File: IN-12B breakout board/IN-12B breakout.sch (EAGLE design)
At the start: 25 parts, among them Q1 500mA/300V, Q10 500mA/300V, Q2 500mA/300V, Q3 500mA/300V, Q4 500mA/300V, Q5 500mA/300V, Q6 500mA/300V, Q7 500mA/300V, Q8 500mA/300V, Q9 500mA/300V

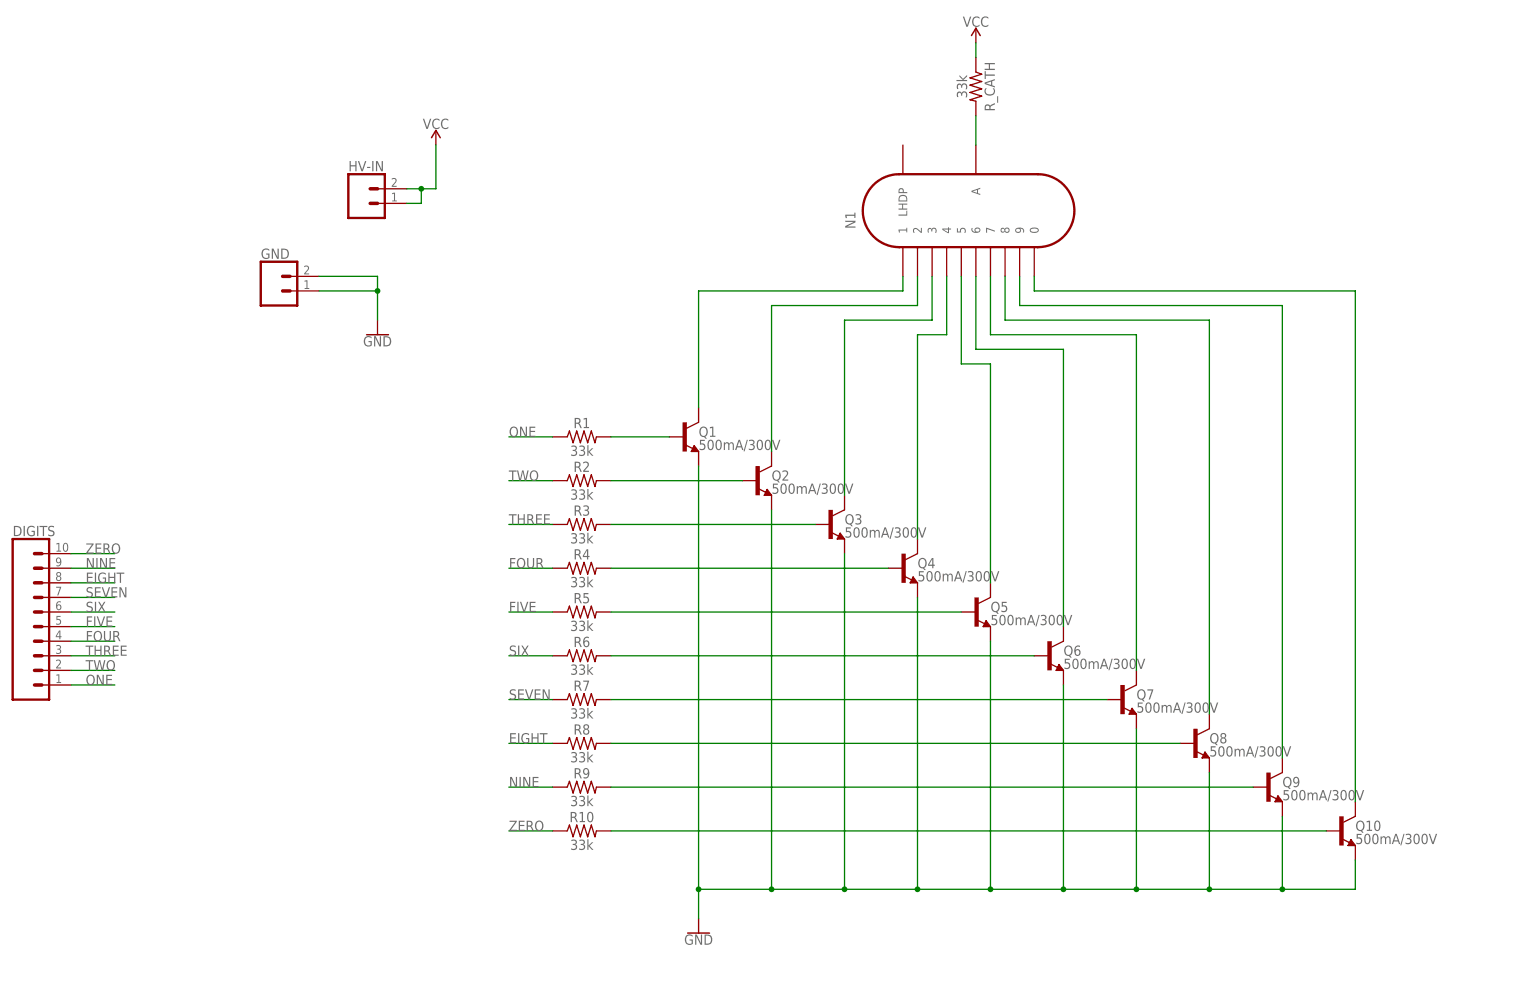
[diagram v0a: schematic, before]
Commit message: board version 2.0, with decimal dot support
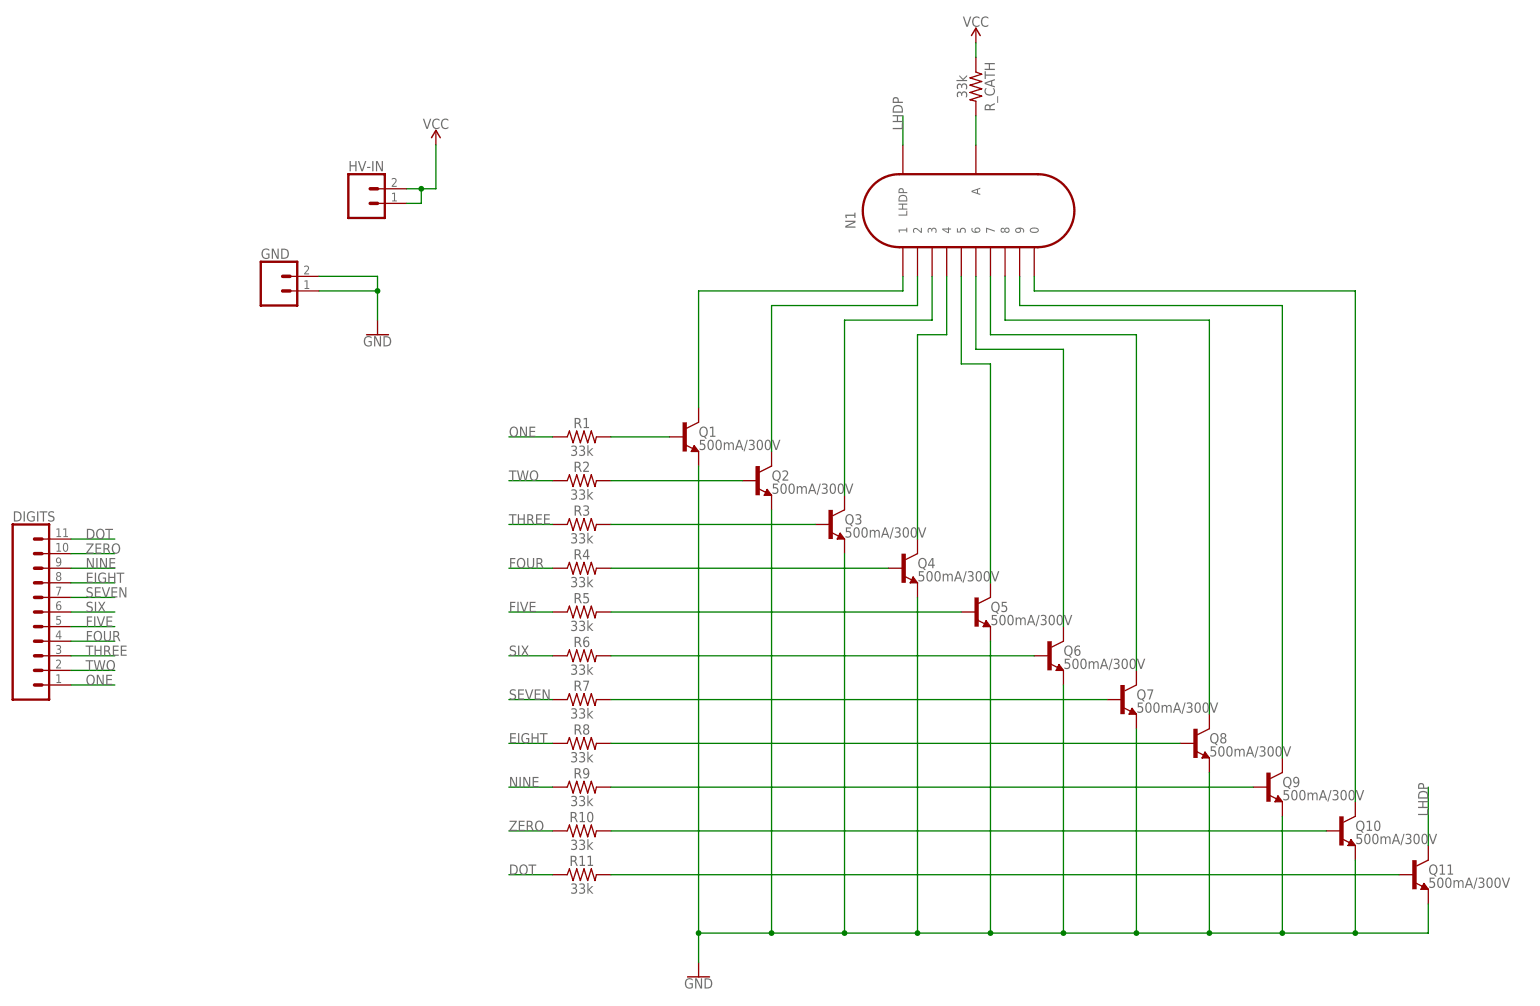
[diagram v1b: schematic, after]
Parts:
- added Q11: 500mA/300V, SparkFun-DiscreteSemi:TRANS_NPN-MMBTA42
- added R11: 33k, SparkFun-Resistors:33KOHM-0603-1/10W-1%
- DIGITS: device SparkFun-Connectors:CONN_10" -> SparkFun-Connectors:CONN_11
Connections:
- new net DOT: DIGITS.11, R11.1
- new net LHDP: N1.LHDP, Q11.C
- new net N$22: Q11.B, R11.2
- net GND: now also Q11.E
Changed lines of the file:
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@@
 <part name="SUPPLY2" library="SparkFun-PowerSymbols" deviceset="VCC" device=""/>
 <part name="R_CATH" library="SparkFun-Resistors" deviceset="33KOHM" device="-0603-1/10W-1%" value="33k"/>
-<part name="DIGITS" library="SparkFun-Connectors" deviceset="CONN_10" device="&quot;"/>
+<part name="DIGITS" library="SparkFun-Connectors" deviceset="CONN_11" device=""/>
 <part name="N1" library="russian-nixies" deviceset="IN-12B" device=""/>
 <part name="GND" library="SparkFun-Connectors" deviceset="CONN_02" device=""/>
 <part name="GND2" library="SparkFun-PowerSymbols" deviceset="GND" device=""/>
+<part name="R11" library="SparkFun-Resistors" deviceset="33KOHM" device="-0603-1/10W-1%" value="33k"/>
+<part name="Q11" library="SparkFun-DiscreteSemi" deviceset="TRANS_NPN" device="-MMBTA42" value="500mA/300V"/>
 </parts>
 <sheets>
@@
 </plain>
 <instances>
-<instance part="GND1" gate="1" x="-17.78" y="10.16"/>
+<instance part="GND1" gate="1" x="-17.78" y="2.54"/>
 <instance part="Q1" gate="G$1" x="-20.32" y="96.52"/>
 <instance part="Q2" gate="G$1" x="-7.62" y="88.9"/>
@@
 <instance part="SUPPLY2" gate="G$1" x="30.48" y="165.1"/>
 <instance part="R_CATH" gate="G$1" x="30.48" y="157.48" rot="R270"/>
-<instance part="DIGITS" gate="G$1" x="-137.16" y="71.12"/>
+<instance part="DIGITS" gate="G$1" x="-137.16" y="66.04"/>
 <instance part="N1" gate="G$1" x="30.48" y="137.16" rot="R90"/>
 <instance part="GND" gate="G$1" x="-91.44" y="121.92"/>
 <instance part="GND2" gate="1" x="-73.66" y="114.3"/>
+<instance part="R11" gate="G$1" x="-38.1" y="20.32"/>
+<instance part="Q11" gate="G$1" x="106.68" y="20.32"/>
 </instances>
 <busses>
@@
 <pinref part="Q1" gate="G$1" pin="E"/>
 <pinref part="GND1" gate="1" pin="GND"/>
-<wire x1="-17.78" y1="91.44" x2="-17.78" y2="17.78" width="0.1524" layer="91"/>
+<wire x1="-17.78" y1="91.44" x2="-17.78" y2="10.16" width="0.1524" layer="91"/>
 <pinref part="Q10" gate="G$1" pin="E"/>
-<wire x1="-17.78" y1="17.78" x2="-17.78" y2="12.7" width="0.1524" layer="91"/>
-<wire x1="-17.78" y1="17.78" x2="-5.08" y2="17.78" width="0.1524" layer="91"/>
-<wire x1="-5.08" y1="17.78" x2="7.62" y2="17.78" width="0.1524" layer="91"/>
-<wire x1="7.62" y1="17.78" x2="20.32" y2="17.78" width="0.1524" layer="91"/>
-<wire x1="20.32" y1="17.78" x2="33.02" y2="17.78" width="0.1524" layer="91"/>
-<wire x1="33.02" y1="17.78" x2="45.72" y2="17.78" width="0.1524" layer="91"/>
-<wire x1="45.72" y1="17.78" x2="58.42" y2="17.78" width="0.1524" layer="91"/>
-<wire x1="58.42" y1="17.78" x2="71.12" y2="17.78" width="0.1524" layer="91"/>
-<wire x1="71.12" y1="17.78" x2="83.82" y2="17.78" width="0.1524" layer="91"/>
-<wire x1="83.82" y1="17.78" x2="96.52" y2="17.78" width="0.1524" layer="91"/>
-<wire x1="96.52" y1="17.78" x2="96.52" y2="22.86" width="0.1524" layer="91"/>
-<junction x="-17.78" y="17.78"/>
+<wire x1="-17.78" y1="10.16" x2="-17.78" y2="5.08" width="0.1524" layer="91"/>
+<wire x1="-17.78" y1="10.16" x2="-5.08" y2="10.16" width="0.1524" layer="91"/>
+<wire x1="-5.08" y1="10.16" x2="7.62" y2="10.16" width="0.1524" layer="91"/>
+<wire x1="7.62" y1="10.16" x2="20.32" y2="10.16" width="0.1524" layer="91"/>
+<wire x1="20.32" y1="10.16" x2="33.02" y2="10.16" width="0.1524" layer="91"/>
+<wire x1="33.02" y1="10.16" x2="45.72" y2="10.16" width="0.1524" layer="91"/>
+<wire x1="45.72" y1="10.16" x2="58.42" y2="10.16" width="0.1524" layer="91"/>
+<wire x1="58.42" y1="10.16" x2="71.12" y2="10.16" width="0.1524" layer="91"/>
+<wire x1="71.12" y1="10.16" x2="83.82" y2="10.16" width="0.1524" layer="91"/>
+<wire x1="83.82" y1="10.16" x2="96.52" y2="10.16" width="0.1524" layer="91"/>
+<wire x1="96.52" y1="10.16" x2="96.52" y2="22.86" width="0.1524" layer="91"/>
+<junction x="-17.78" y="10.16"/>
 <pinref part="Q9" gate="G$1" pin="E"/>
-<wire x1="83.82" y1="30.48" x2="83.82" y2="17.78" width="0.1524" layer="91"/>
-<junction x="83.82" y="17.78"/>
+<wire x1="83.82" y1="30.48" x2="83.82" y2="10.16" width="0.1524" layer="91"/>
+<junction x="83.82" y="10.16"/>
 <pinref part="Q8" gate="G$1" pin="E"/>
-<wire x1="71.12" y1="38.1" x2="71.12" y2="17.78" width="0.1524" layer="91"/>
-<junction x="71.12" y="17.78"/>
+<wire x1="71.12" y1="38.1" x2="71.12" y2="10.16" width="0.1524" layer="91"/>
+<junction x="71.12" y="10.16"/>
 <pinref part="Q7" gate="G$1" pin="E"/>
-<wire x1="58.42" y1="45.72" x2="58.42" y2="17.78" width="0.1524" layer="91"/>
-<junction x="58.42" y="17.78"/>
+<wire x1="58.42" y1="45.72" x2="58.42" y2="10.16" width="0.1524" layer="91"/>
+<junction x="58.42" y="10.16"/>
 <pinref part="Q6" gate="G$1" pin="E"/>
-<wire x1="45.72" y1="53.34" x2="45.72" y2="17.78" width="0.1524" layer="91"/>
-<junction x="45.72" y="17.78"/>
+<wire x1="45.72" y1="53.34" x2="45.72" y2="10.16" width="0.1524" layer="91"/>
+<junction x="45.72" y="10.16"/>
 <pinref part="Q5" gate="G$1" pin="E"/>
-<wire x1="33.02" y1="60.96" x2="33.02" y2="17.78" width="0.1524" layer="91"/>
-<junction x="33.02" y="17.78"/>
+<wire x1="33.02" y1="60.96" x2="33.02" y2="10.16" width="0.1524" layer="91"/>
+<junction x="33.02" y="10.16"/>
 <pinref part="Q4" gate="G$1" pin="E"/>
-<wire x1="20.32" y1="68.58" x2="20.32" y2="17.78" width="0.1524" layer="91"/>
-<junction x="20.32" y="17.78"/>
+<wire x1="20.32" y1="68.58" x2="20.32" y2="10.16" width="0.1524" layer="91"/>
+<junction x="20.32" y="10.16"/>
 <pinref part="Q3" gate="G$1" pin="E"/>
-<wire x1="7.62" y1="76.2" x2="7.62" y2="17.78" width="0.1524" layer="91"/>
-<junction x="7.62" y="17.78"/>
+<wire x1="7.62" y1="76.2" x2="7.62" y2="10.16" width="0.1524" layer="91"/>
+<junction x="7.62" y="10.16"/>
 <pinref part="Q2" gate="G$1" pin="E"/>
-<wire x1="-5.08" y1="83.82" x2="-5.08" y2="17.78" width="0.1524" layer="91"/>
-<junction x="-5.08" y="17.78"/>
+<wire x1="-5.08" y1="83.82" x2="-5.08" y2="10.16" width="0.1524" layer="91"/>
+<junction x="-5.08" y="10.16"/>
+<pinref part="Q11" gate="G$1" pin="E"/>
+<wire x1="109.22" y1="15.24" x2="109.22" y2="10.16" width="0.1524" layer="91"/>
+<wire x1="109.22" y1="10.16" x2="96.52" y2="10.16" width="0.1524" layer="91"/>
+<junction x="96.52" y="10.16"/>
 </segment>
 <segment>
@@
 </segment>
 </net>
+<net name="DOT" class="0">
+<segment>
+<pinref part="DIGITS" gate="G$1" pin="11"/>
+<wire x1="-127" y1="78.74" x2="-119.38" y2="78.74" width="0.1524" layer="91"/>
+<label x="-124.46" y="78.74" size="1.778" layer="95"/>
+</segment>
+<segment>
+<pinref part="R11" gate="G$1" pin="1"/>
+<wire x1="-43.18" y1="20.32" x2="-50.8" y2="20.32" width="0.1524" layer="91"/>
+<label x="-50.8" y="20.32" size="1.778" layer="95"/>
+</segment>
+</net>
+<net name="N$22" class="0">
+<segment>
+<pinref part="Q11" gate="G$1" pin="B"/>
+<wire x1="104.14" y1="20.32" x2="-33.02" y2="20.32" width="0.1524" layer="91"/>
+<pinref part="R11" gate="G$1" pin="2"/>
+</segment>
+</net>
+<net name="LHDP" class="0">
+<segment>
+<pinref part="Q11" gate="G$1" pin="C"/>
+<wire x1="109.22" y1="25.4" x2="109.22" y2="35.56" width="0.1524" layer="91"/>
+<label x="109.22" y="30.48" size="1.778" layer="95" rot="R90"/>
+</segment>
+<segment>
+<pinref part="N1" gate="G$1" pin="LHDP"/>
+<wire x1="17.78" y1="147.32" x2="17.78" y2="152.4" width="0.1524" layer="91"/>
+<label x="17.78" y="149.86" size="1.778" layer="95" rot="R90"/>
+</segment>
+</net>
